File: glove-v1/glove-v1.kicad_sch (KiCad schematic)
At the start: 22 parts, among them J1 Conn_01x05, Q1 Q_PMOS_GSD, Q2 Q_Photo_NPN_EC, SW1 SW_Push, U1 LIS3DH, U2 STM32L031G6Ux

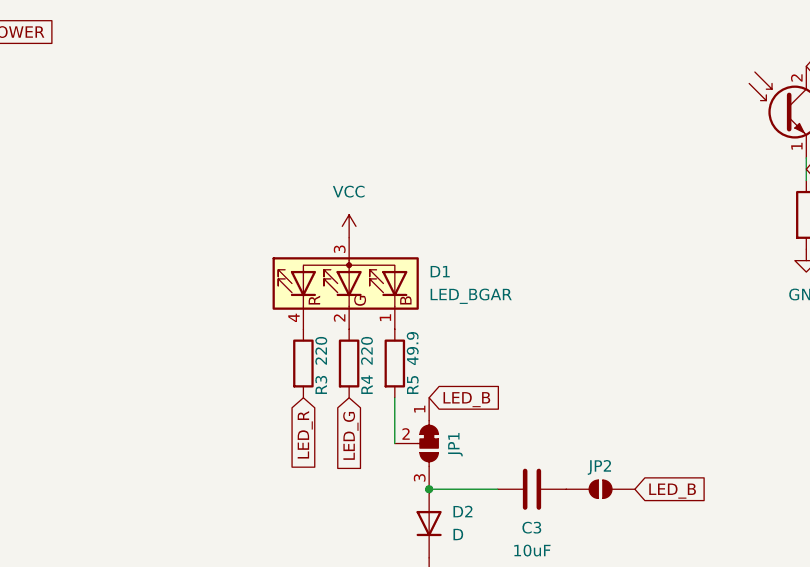
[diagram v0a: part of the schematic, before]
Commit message: fibonacci64: first version!
I produced this, and it works at least partially. The code is copied
from earring-ring-rgb36 which lights up around half the LEDs.

There's a few things that need changes though.
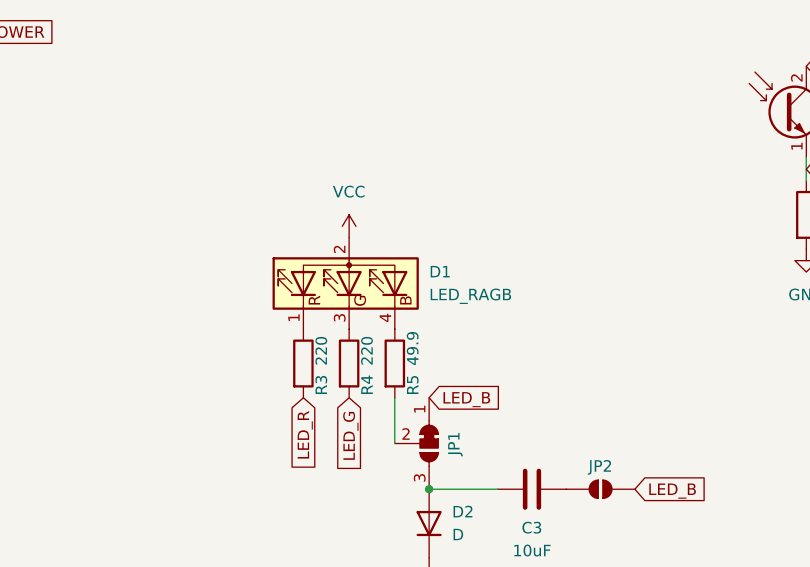
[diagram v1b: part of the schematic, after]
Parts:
- removed D1: LED_BGAR, Custom:OSRAM_KRTB_AILMS1, symbol Device:LED_BGAR
- added D1: LED_RAGB, symbol Device:LED_RAGB
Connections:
- net VCC: now also D1.2 (A)
- net at U1.2 (BYP): now also C4.1
- net at R5.1: now also D1.4 (BK)
- net at R4.1: now also D1.3 (GK)
- net at R3.1: now also D1.1 (RK)
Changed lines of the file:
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@@
-	)
-	(symbol
-		(lib_id "Device:LED_BGAR")
-		(at 128.27 100.33 90)
-		(unit 1)
-		(exclude_from_sim no)
-		(in_bom yes)
-		(on_board yes)
-		(dnp no)
-		(fields_autoplaced yes)
-		(property "Reference" "D1"
-			(at 137.16 99.0599 90)
-			(effects
-				(font
-					(size 1.27 1.27)
-				)
-				(justify right)
-			)
-		)
-		(property "Value" "LED_BGAR"
-			(at 137.16 101.5999 90)
-			(effects
-				(font
-					(size 1.27 1.27)
-				)
-				(justify right)
-			)
-		)
-		(property "Footprint" "Custom:OSRAM_KRTB_AILMS1"
-			(at 129.54 100.33 0)
-			(effects
-				(font
-					(size 1.27 1.27)
-				)
-				(hide yes)
-			)
-		)
-		(property "Datasheet" "~"
-			(at 129.54 100.33 0)
-			(effects
-				(font
-					(size 1.27 1.27)
-				)
-				(hide yes)
-			)
-		)
-		(property "Description" "RGB LED, blue/green/anode/red"
-			(at 128.27 100.33 0)
-			(effects
-				(font
-					(size 1.27 1.27)
-				)
-				(hide yes)
-			)
-		)
-		(property "LCSC" "C7212758"
-			(at 128.27 100.33 90)
-			(effects
-				(font
-					(size 1.27 1.27)
-				)
-				(hide yes)
-			)
-		)
-		(pin "4"
-		)
-		(pin "2"
-		)
-		(pin "3"
-		)
-		(pin "1"
-		)
-		(instances
-			(project ""
-				(path "/90549a1f-9455-4729-b73f-f032fe2e8ad5"
-					(reference "D1")
-					(unit 1)
-				)
-			)
-		)
 	)
 	(symbol
@@
 					(unit 1)
 				)
+			)
+		)
+	)
+	(symbol
+		(lib_id "Device:LED_RAGB")
+		(at 128.27 100.33 90)
+		(unit 1)
+		(exclude_from_sim no)
+		(in_bom yes)
+		(on_board yes)
+		(dnp no)
+		(fields_autoplaced yes)
+		(property "Reference" "D1"
+			(at 137.16 99.0599 90)
+			(effects
+				(font
+					(size 1.27 1.27)
+				)
+				(justify right)
+			)
+		)
+		(property "Value" "LED_RAGB"
+			(at 137.16 101.5999 90)
+			(effects
+				(font
+					(size 1.27 1.27)
+				)
+				(justify right)
+			)
+		)
+		(property "Footprint" ""
+			(at 129.54 100.33 0)
+			(effects
+				(font
+					(size 1.27 1.27)
+				)
+				(hide yes)
+			)
+		)
+		(property "Datasheet" "~"
+			(at 129.54 100.33 0)
+			(effects
+				(font
+					(size 1.27 1.27)
+				)
+				(hide yes)
+			)
+		)
+		(property "Description" "RGB LED, red/anode/green/blue"
+			(at 128.27 100.33 0)
+			(effects
+				(font
+					(size 1.27 1.27)
+				)
+				(hide yes)
+			)
+		)
+		(pin "1"
+		)
+		(pin "4"
+		)
+		(pin "3"
+		)
+		(pin "2"
+		)
+		(instances
+			(project ""
+				(path "/90549a1f-9455-4729-b73f-f032fe2e8ad5"
+					(reference "D1")
+					(unit 1)
+				)
